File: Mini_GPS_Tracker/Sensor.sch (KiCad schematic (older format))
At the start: 2 parts, among them U5 MS5611-01BA

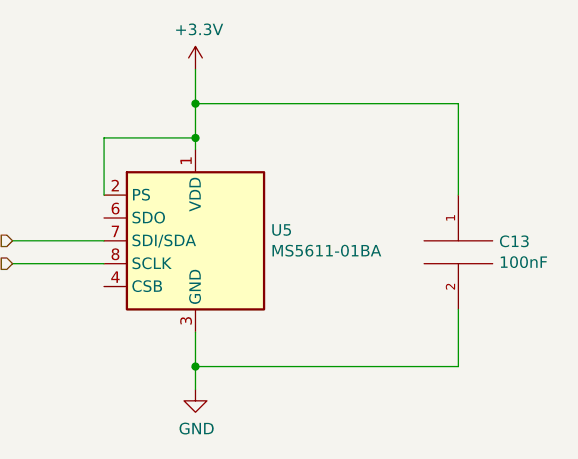
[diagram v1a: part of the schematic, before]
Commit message: updated antenna;
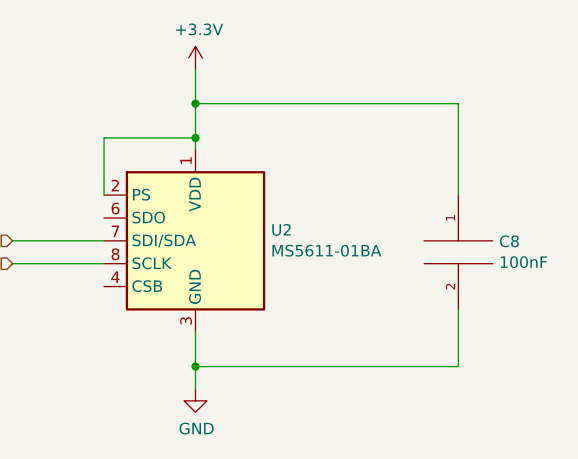
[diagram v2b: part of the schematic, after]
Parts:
- renumbered C13 to C8, U5 to U2
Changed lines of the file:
@@
 $EndDescr
 $Comp
-L Sensor_Pressure:MS5611-01BA U5
+L Sensor_Pressure:MS5611-01BA U2
 U 1 1 5E6E6D79
 P 5000 3500
-F 0 "U5" H 5330 3546 50  0000 L CNN
+F 0 "U2" H 5330 3546 50  0000 L CNN
 F 1 "MS5611-01BA" H 5330 3455 50  0000 L CNN
 F 2 "Package_LGA:LGA-8_3x5mm_P1.25mm" H 5000 3500 50  0001 C CNN
@@
 	4200 3500 4600 3500
 $Comp
-L power:GND #PWR0124
+L power:GND #PWR017
 U 1 1 5E6E7BFC
 P 5000 4150
-F 0 "#PWR0124" H 5000 3900 50  0001 C CNN
+F 0 "#PWR017" H 5000 3900 50  0001 C CNN
 F 1 "GND" H 5005 3977 50  0000 C CNN
 F 2 "" H 5000 4150 50  0001 C CNN
@@
 $EndComp
 $Comp
-L power:+3.3V #PWR0125
+L power:+3.3V #PWR016
 U 1 1 5E6E8AC2
 P 5000 2750
-F 0 "#PWR0125" H 5000 2600 50  0001 C CNN
+F 0 "#PWR016" H 5000 2600 50  0001 C CNN
 F 1 "+3.3V" H 5015 2923 50  0000 C CNN
 F 2 "" H 5000 2750 50  0001 C CNN
@@
 $EndComp
 $Comp
-L pspice:CAP C13
+L pspice:CAP C8
 U 1 1 5E6E943F
 P 6150 3550
-F 0 "C13" H 6328 3596 50  0000 L CNN
+F 0 "C8" H 6328 3596 50  0000 L CNN
 F 1 "100nF" H 6328 3505 50  0000 L CNN
 F 2 "Capacitor_SMD:C_0805_2012Metric_Pad1.15x1.40mm_HandSolder" H 6150 3550 50  0001 C CNN

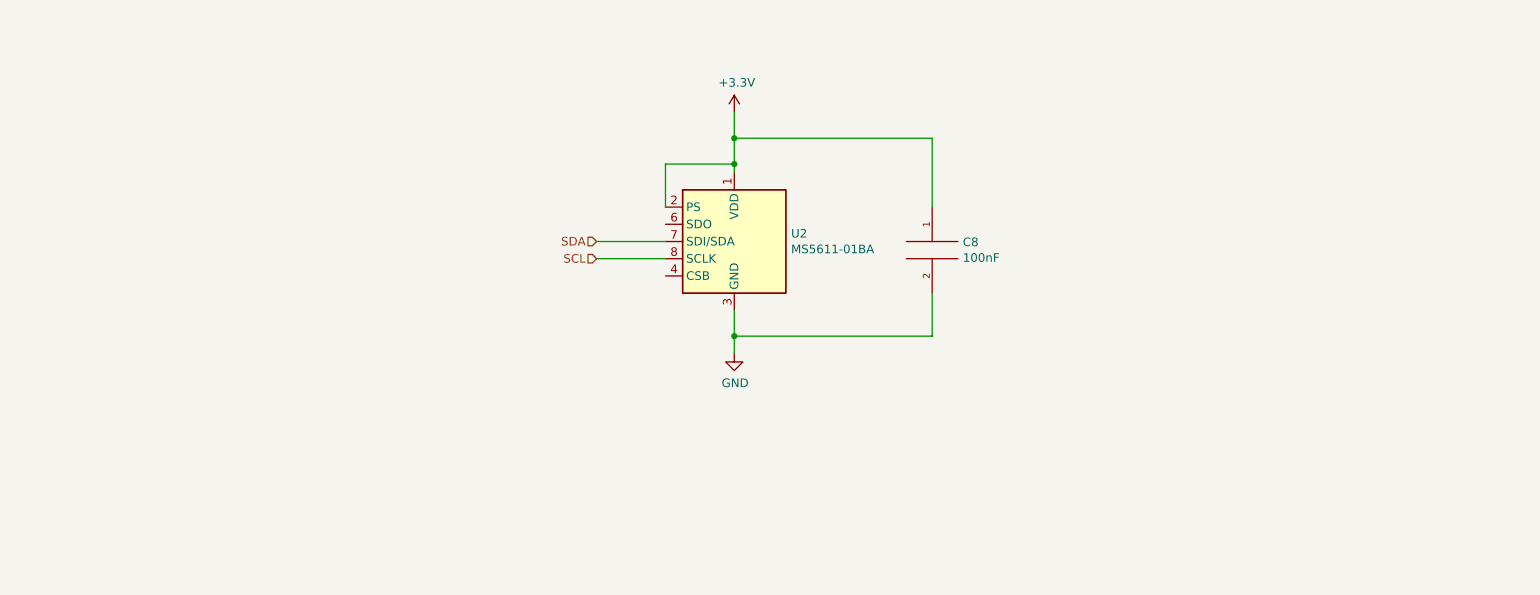
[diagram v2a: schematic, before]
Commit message: added 9dof
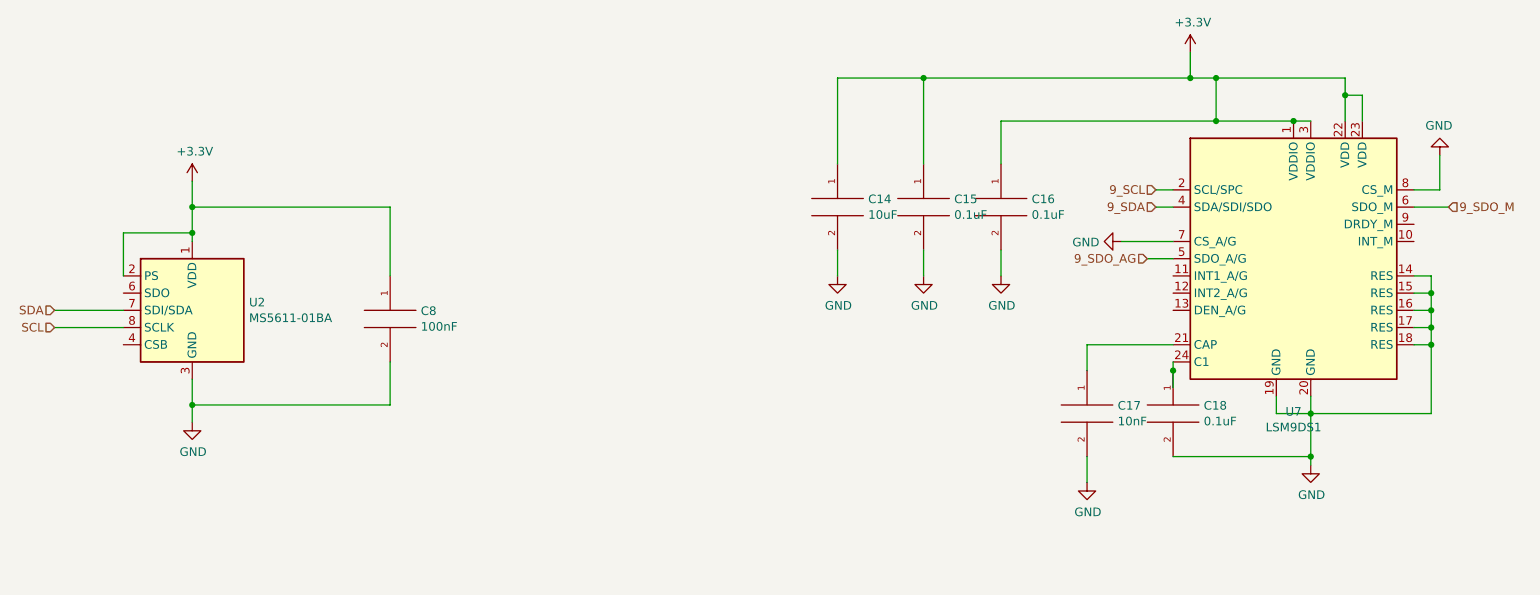
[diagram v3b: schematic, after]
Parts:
- added C14: 10uF, Capacitor_SMD:C_0805_2012Metric_Pad1.15x1.40mm_HandSolder, symbol pspice:CAP
- added C15, C16, C18: 0.1uF, Capacitor_SMD:C_0805_2012Metric_Pad1.15x1.40mm_HandSolder, symbol pspice:CAP
- added C17: 10nF, Capacitor_SMD:C_0805_2012Metric_Pad1.15x1.40mm_HandSolder, symbol pspice:CAP
- added U7: LSM9DS1, Package_LGA:LGA-24L_3x3.5mm_P0.43mm, symbol Sensor_Motion:LSM9DS1
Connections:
- net +3V3: now also C14.1, C15.1, C16.1, U7.1 (VDDIO), U7.22 (VDD), U7.23 (VDD), U7.3 (VDDIO)
- net GND: now also C14.2, C15.2, C16.2, C17.2, C18.2, U7.14 (RES), U7.15 (RES), U7.16 (RES), U7.17 (RES), U7.18 (RES), U7.19 (GND), U7.20 (GND), U7.7 (CS_A/G), U7.8 (CS_M)
- new net: C17.1, U7.21 (CAP)
- new net: C18.1, U7.24 (C1)
- new net 9_SCL: U7.2 (SCL/SPC)
- new net 9_SDA: U7.4 (SDA/SDI/SDO)
- new net 9_SDO_AG: U7.5 (SDO_A/G)
- new net 9_SDO_M: U7.6 (SDO_M)
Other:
- moved on the sheet: C8, U2

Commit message: schamatics finalized
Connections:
- net 9_SDO_AG is gone; now on net +3V3: U7.5 (SDO_A/G)
- net 9_SDO_M is gone; now on net +3V3: U7.6 (SDO_M)
- no-connect marks 0 -> 7
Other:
- moved on the sheet: C14, C15, C16, C17, C18, U7
